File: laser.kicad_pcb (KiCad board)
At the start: 4 copper layers, 90.2 x 50.9 mm, 127 parts, among them IC201 ADM7172ACPZ-4.2-R7, IC202 LT1716CS5#TRPBF, IC203 ADM7154ARDZ-3.3-R7, IC204 IRF9358PBF, IC601 ATMEGA328P-AU, IC602 FT232RL-TUBE, IC701 MAX6126AASA25+, IC801 ADS122C04IPWR, J601 M20-9980345, J602 USB_Connector, Q401 RSR030N06TL, U101 281698-3, U201 LM4040EIM3X-2.5_NOPB, U301 OPA569AIDWPR, U302 OPA569AIDWPR, U401 ADA4528-2ACPZ-RL, U402 782853152_WE-CBA_08, U501 ADA4528-2ACPZ-RL, U502 ADA4528-2ACPZ-RL, U801 MAX5217GUA+, U802 MAX5217GUA+, Y601 ECS-160-16-33B-CKM-TR

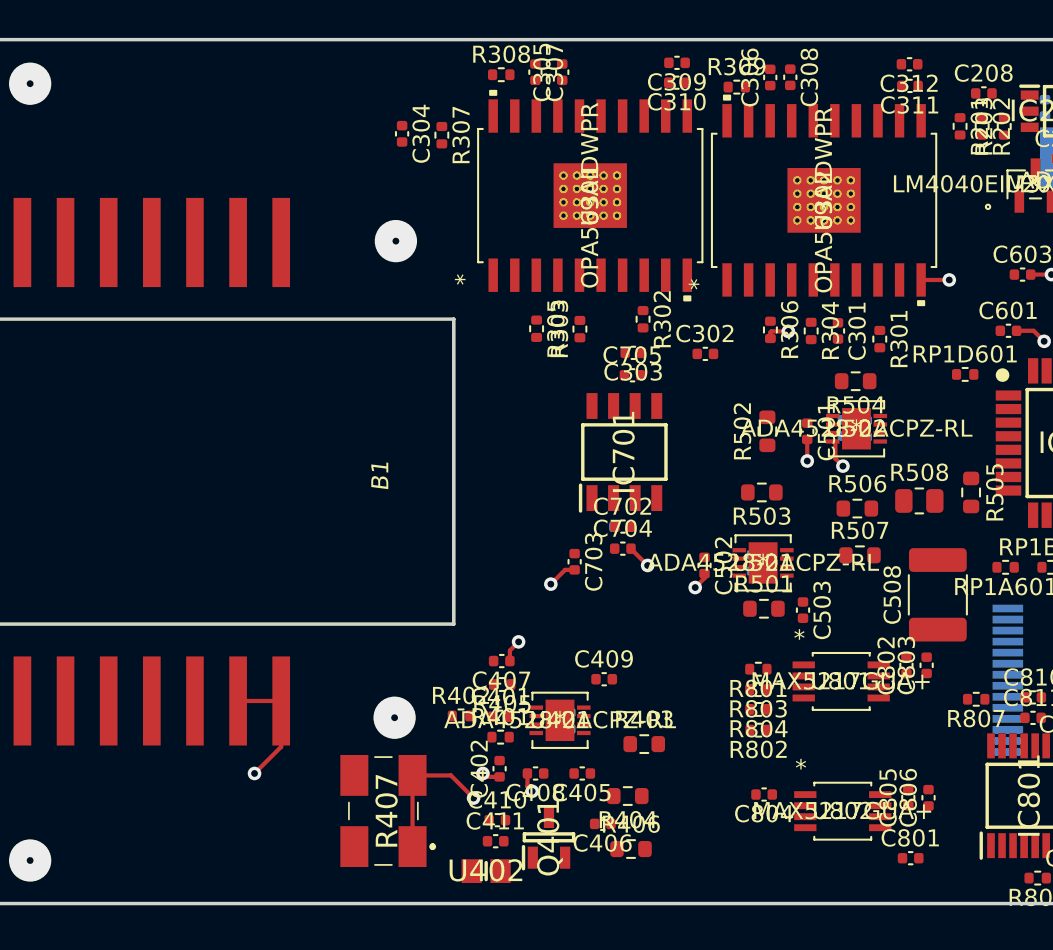
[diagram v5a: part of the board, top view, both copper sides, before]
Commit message: connect all opa pads to ground
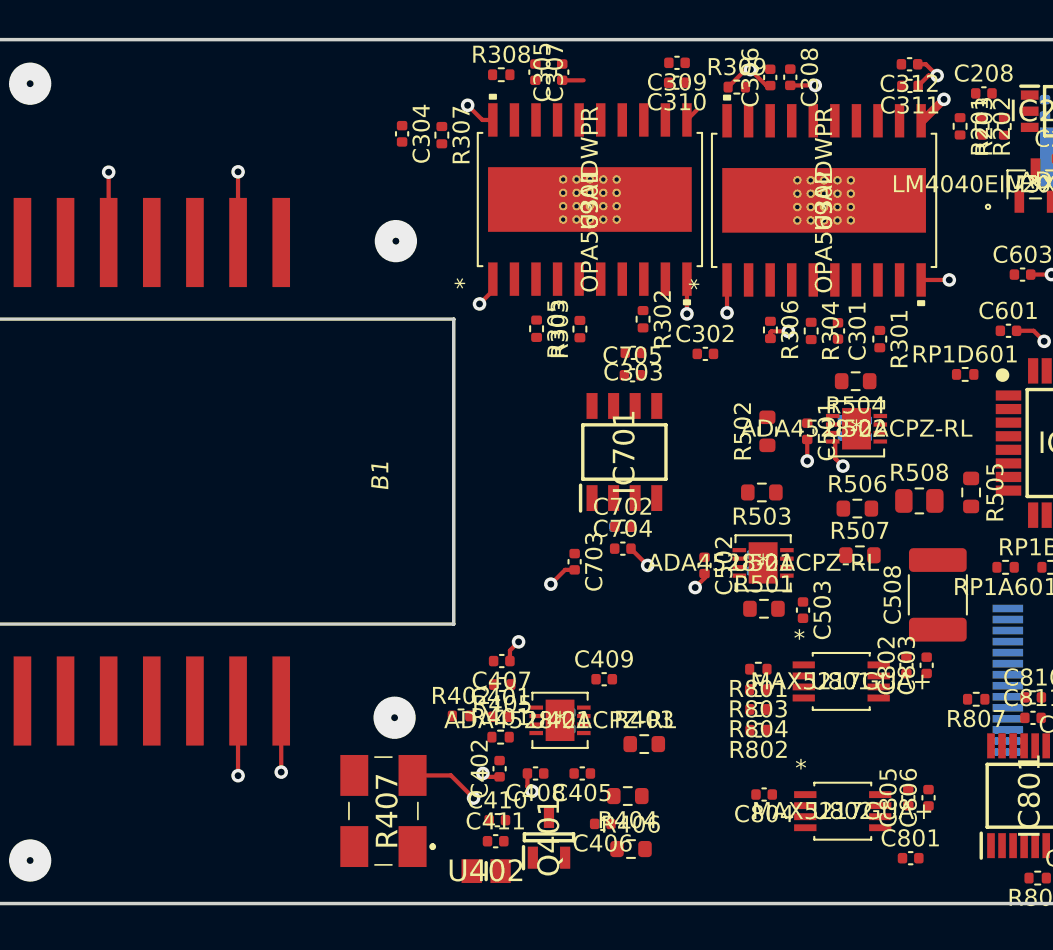
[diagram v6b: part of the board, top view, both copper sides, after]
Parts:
- moved U301 0.23 mm to (163.8, 90.8)
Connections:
- U301 pad V: (no net) -> GND
- U302 pad V: (no net) -> GND
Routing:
- net GND: track 73.7 -> 98.8 mm, vias 18 -> 37
- net (no net): vias 8 -> 0

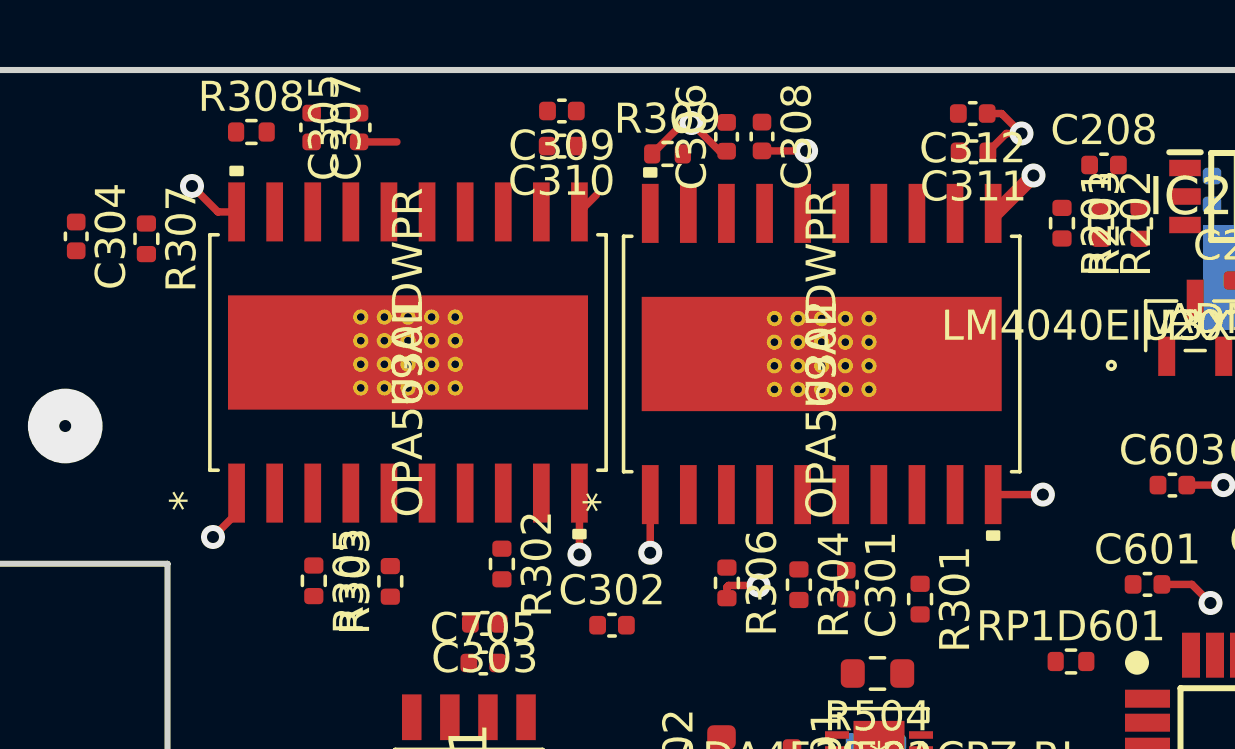
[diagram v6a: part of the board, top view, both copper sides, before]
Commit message: make traces 0.5 mm
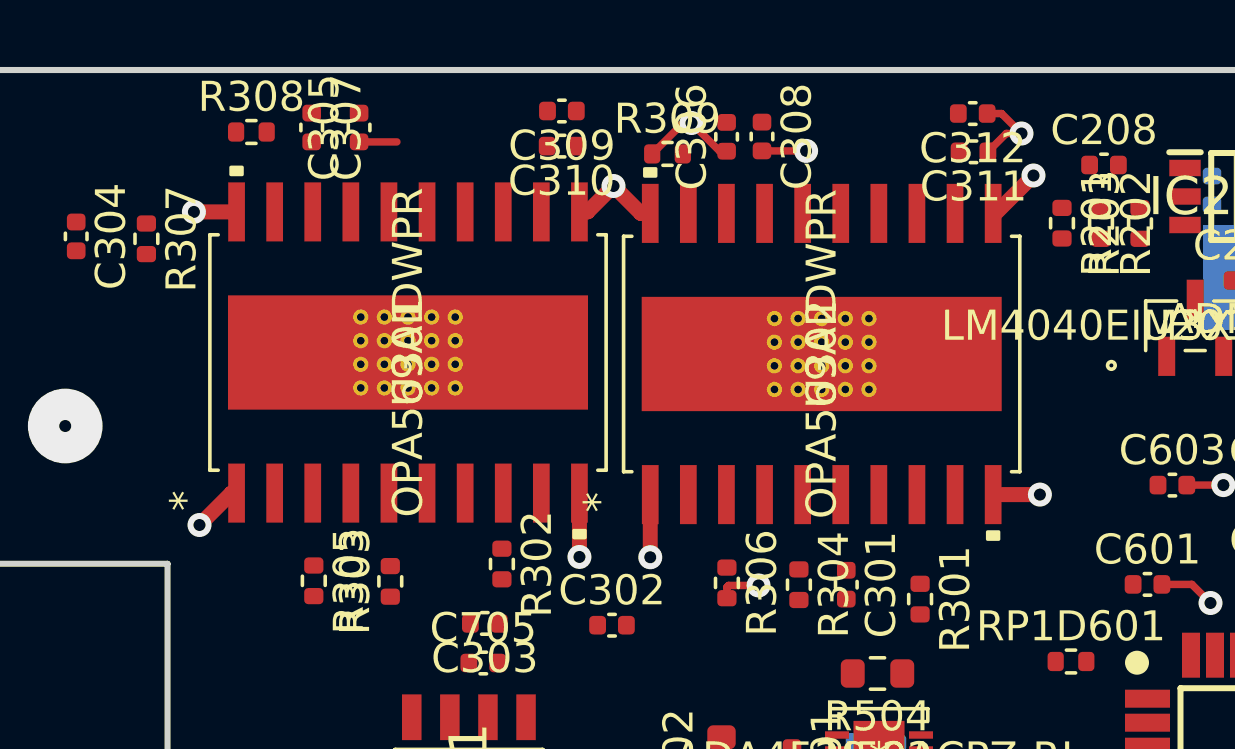
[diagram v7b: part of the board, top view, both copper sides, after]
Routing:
- net GND: track 98.8 -> 100.4 mm, vias 37 -> 38

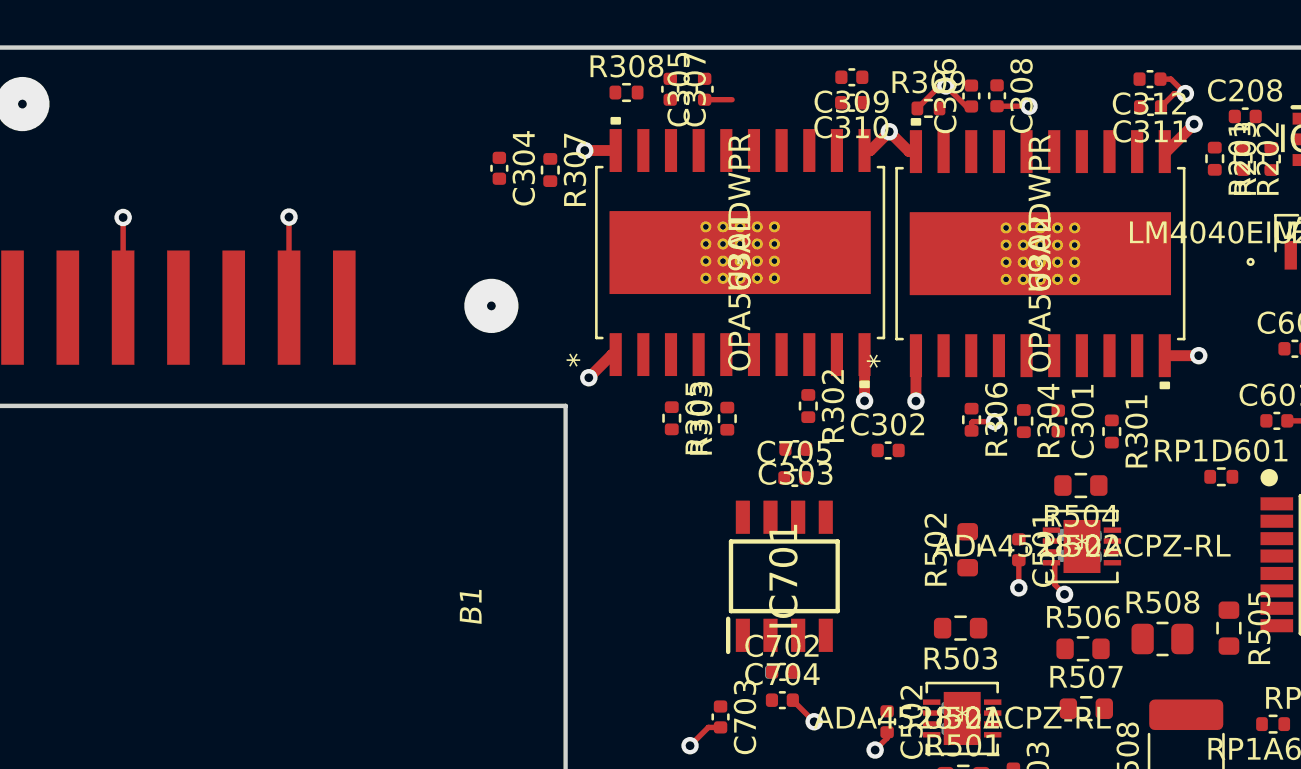
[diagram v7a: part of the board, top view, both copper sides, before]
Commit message: grounded epad on pcb
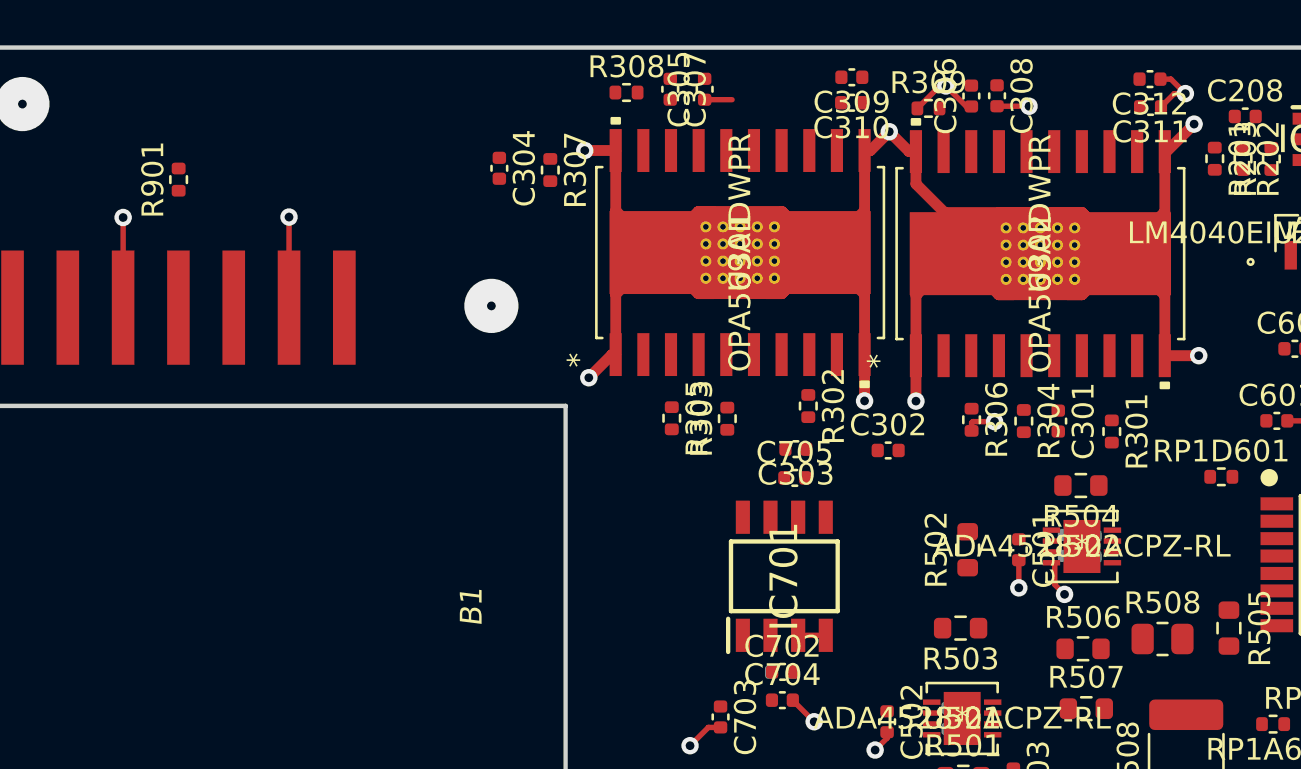
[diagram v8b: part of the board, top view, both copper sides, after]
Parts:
- added R901: 100k, Resistor_SMD:R_0402_1005Metric, F.Cu at (138.0, 87.4)
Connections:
- IC203 pad 9: Net-(IC203-Pad9) -> GND
- U301 pad EPAD: Net-(U301-PadEPAD) -> GND
- U301 pad V: GND -> (no net)
- U302 pad EPAD: Net-(U302-PadEPAD) -> GND
- U302 pad V: GND -> (no net)
- U501 pad 9: Net-(U501-Pad9) -> GND
- U502 pad 9: Net-(U502-Pad9) -> GND
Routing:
- net GND: track 100.4 -> 208.4 mm
